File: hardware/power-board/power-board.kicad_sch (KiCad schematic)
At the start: 0 parts

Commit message: Segregated specific libs into shared libs
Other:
- added sheet BMS (bms.kicad_sch)
- added sheet Charger (charger.kicad_sch)
- added sheet Control (control.kicad_sch)
- added sheet Hotswap (hotswap.kicad_sch)
- added sheet Hotswap1 (hotswap.kicad_sch)
- added sheet Supplies (supplies.kicad_sch)

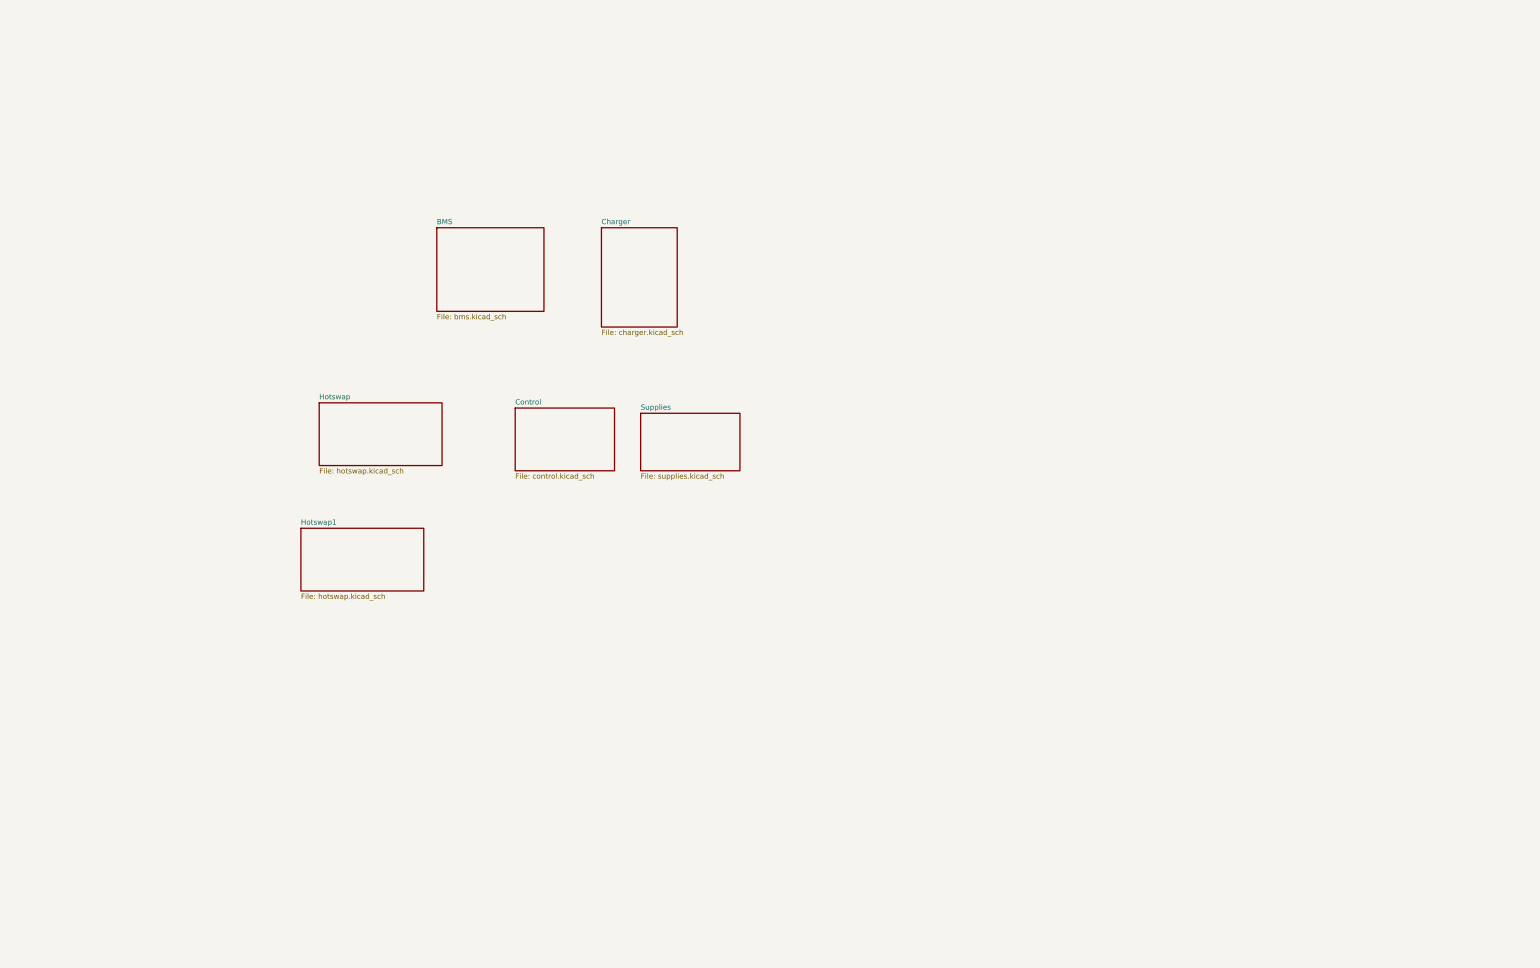
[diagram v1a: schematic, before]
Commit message: Added more ICs for power board
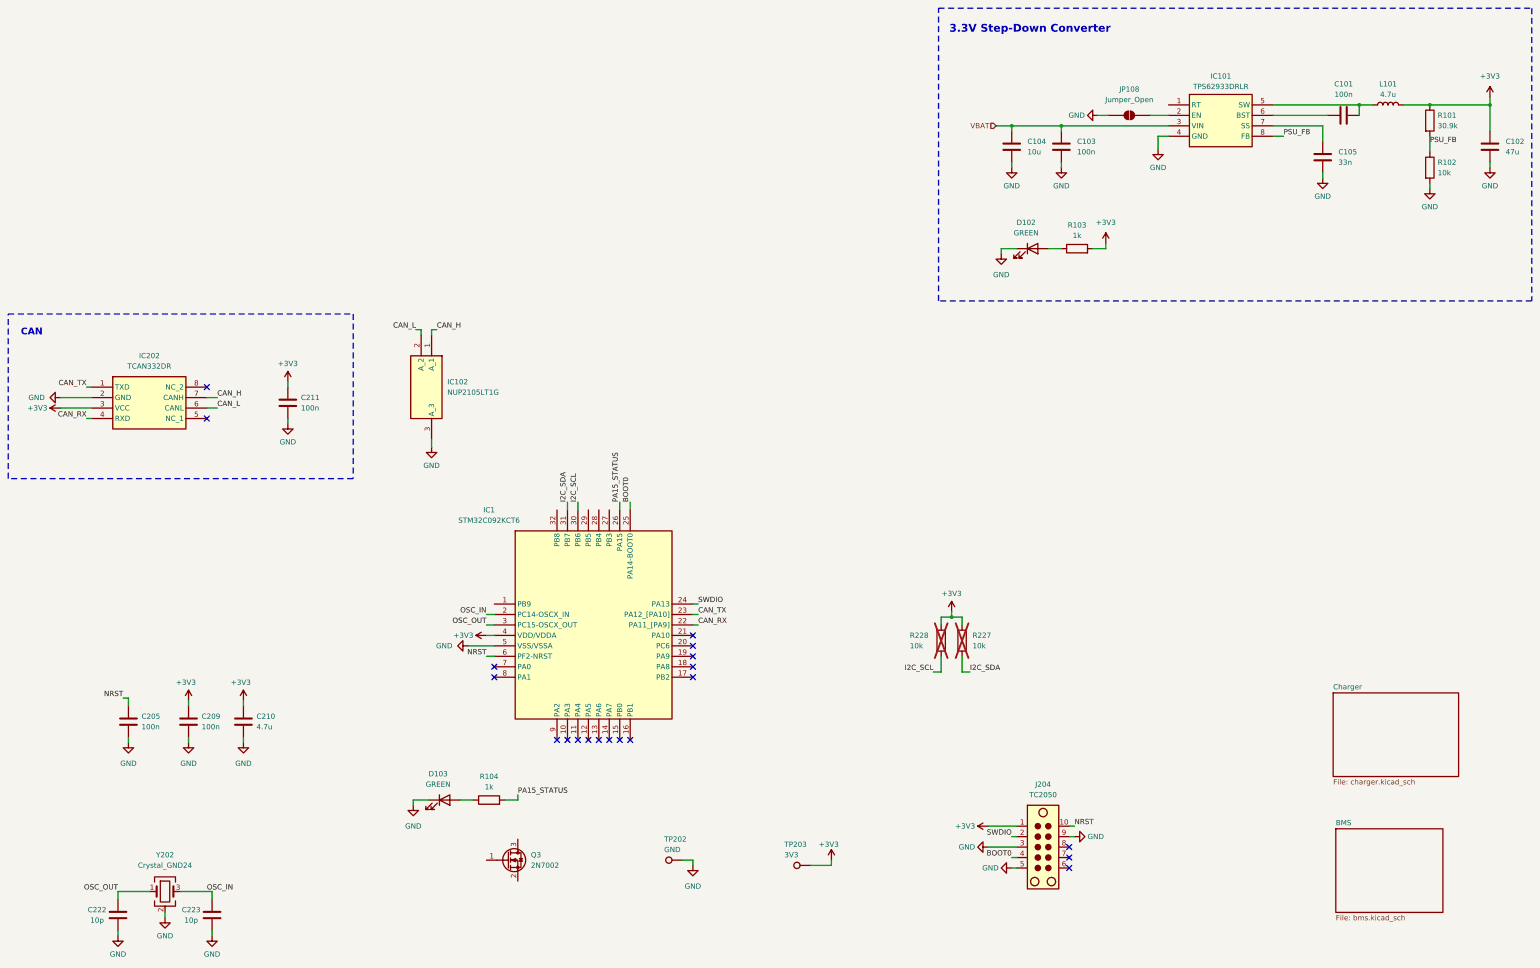
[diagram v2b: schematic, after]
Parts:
- added C101, C103, C205, C209, C211: 100n, Capacitor_SMD:C_0805_2012Metric, symbol Device:C
- added C102: 47u, Capacitor_SMD:C_0805_2012Metric, symbol Device:C
- added C104: 10u, Capacitor_SMD:C_0805_2012Metric, symbol Device:C
- added C105: 33n, Capacitor_SMD:C_0805_2012Metric, symbol Device:C
- added C210: 4.7u, Capacitor_SMD:C_0805_2012Metric, symbol Device:C
- added C222, C223: 10p, Capacitor_SMD:C_0805_2012Metric, symbol Device:C
- added D102, D103: GREEN, LED_SMD:LED_0805_2012Metric, symbol Device:LED
- added IC1: STM32C092KCT6, vector:QFP80P900X900X160-32N, symbol vector:STM32C092KCT6
- added IC101: TPS62933DRLR, vector:SOTFL50P160X60-8N, symbol vector:TPS62933DRLR
- added IC102: NUP2105LT1G, vector:SOT96P237X111-3N, symbol vector:NUP2105LT1G
- added IC202: TCAN332DR, vector:SOIC127P600X175-8N, symbol vector:TCAN332DR
- added J204: TC2050, Connector:Tag-Connect_TC2050-IDC-FP_2x05_P1.27mm_Vertical, symbol Connector:TC2050
- added JP108: Jumper_Open, Jumper:SolderJumper-2_P1.3mm_Open_Pad1.0x1.5mm, symbol Jumper:SolderJumper_2_Open
- added L101: 4.7u, symbol Device:L
- added Q3: 2N7002, Package_TO_SOT_SMD:SOT-23, symbol Transistor_FET:2N7002
- added R101: 30.9k, Resistor_SMD:R_0805_2012Metric, symbol Device:R
- added R102: 10k, Resistor_SMD:R_0805_2012Metric, symbol Device:R
- added R103, R104: 1k, Resistor_SMD:R_0603_1608Metric, symbol Device:R
- added R227, R228: 10k, Resistor_SMD:R_0603_1608Metric, symbol Device:R
- added TP202: GND, TestPoint:TestPoint_Pad_D2.0mm, symbol Connector:TestPoint
- added TP203: 3V3, TestPoint:TestPoint_Pad_D2.0mm, symbol Connector:TestPoint
- added Y202: Crystal_GND24, Crystal:Crystal_SMD_2016-4Pin_2.0x1.6mm, symbol Device:Crystal_GND24
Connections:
- new net: C101.1, IC101.6 (BST)
- new net: C101.2, IC101.5 (SW), L101.1
- new net: D102.2 (A), R103.1
- new net: IC101.2 (EN), JP108.2 (B)
- new net: C105.2, IC101.7 (SS)
- new net: D103.2 (A), R104.1
- new net +3V3: C102.2, C209.2, C210.2, C211.2, IC1.4 (VDD/VDDA), IC202.3 (VCC), J204.1, L101.2, R101.1, R103.2, R227.2, R228.1, TP203.1
- new net BOOT0: IC1.25 (PA14-BOOT0), J204.4
- new net CAN_H: IC102.1 (A_1), IC202.7 (CANH)
- new net CAN_L: IC102.2 (A_2), IC202.6 (CANL)
- new net CAN_RX: IC1.22 (PA11_[PA9]), IC202.4 (RXD)
- new net CAN_TX: IC1.23 (PA12_[PA10]), IC202.1 (TXD)
- new net GND: C102.1, C103.1, C104.1, C105.1, C205.1, C209.1, C210.1, C211.1, C222.1, C223.1, D102.1 (K), D103.1 (K), IC1.5 (VSS/VSSA), IC101.4 (GND), IC102.3 (A_3), IC202.2 (GND), J204.3, J204.5, J204.9, JP108.1 (A), R102.2, TP202.1, Y202.2 (G), Y202.4 (G)
- new net I2C_SCL: IC1.30 (PB6), R228.2
- new net I2C_SDA: IC1.31 (PB7), R227.1
- new net NRST: C205.2, IC1.6 (PF2-NRST), J204.10
- new net OSC_IN: C223.2, IC1.2 (PC14-OSCX_IN), Y202.3
- new net OSC_OUT: C222.2, IC1.3 (PC15-OSCX_OUT), Y202.1
- new net PA15_STATUS: IC1.26 (PA15), R104.2
- new net PSU_FB: IC101.8 (FB), R101.2, R102.1
- new net SWDIO: IC1.24 (PA13), J204.2
- new net VBAT: C103.2, C104.2, IC101.3 (VIN)
- no-connect marks 0 -> 20
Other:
- removed sheet Control
- removed sheet Hotswap
- removed sheet Hotswap1
- removed sheet Supplies
- note added: "3.3V Step-Down Converter"
- note added: "CAN"

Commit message: draw power board bms, charger and mcu circuits
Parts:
- added J501: CAN, Connector_JST:JST_GH_SM04B-GHS-TB_1x04-1MP_P1.25mm_Horizontal, symbol Connector_Generic:Conn_01x04
- added J502: SYSCTL, Connector_JST:JST_GH_SM06B-GHS-TB_1x06-1MP_P1.25mm_Horizontal, symbol Connector_Generic:Conn_01x06
- added R501, R503: 100k, Resistor_SMD:R_0603_1608Metric, symbol Device:R
- added R502: 100, Resistor_SMD:R_0603_1608Metric, symbol Device:R
- added R504, R505, R506, R507: 10k, Resistor_SMD:R_0603_1608Metric, symbol Device:R
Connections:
- net +3V3: now also R504.1, R505.1, R506.1, R507.1
- net CAN_H: now also J501.1 (Pin_1)
- net CAN_L: now also J501.2 (Pin_2)
- net GND: now also Q3.2 (S), J501.3 (Pin_3), J502.1 (Pin_1), R501.2, R503.2
- net REG1: now reaches IC101.2 (EN), JP108.2 (B)
- net 5V_PG: now reaches IC1.13 (PA6)
- net 5V_PG: now also J502.6 (Pin_6), R504.2
- net CM5_OFF: now reaches IC1.15 (PB0)
- net CM5_OFF: now also Q3.1 (G), R501.1
- net BMS_ALERT: now reaches IC1.16 (PB1)
- net BMS_ALERT: now also R506.2
- net CHG_INT: now reaches IC1.17 (PB2)
- net CHG_INT: now also R505.2
- net MCU_ESTOP_N: now reaches IC1.18 (PA8)
- net MCU_ESTOP_N: now also R502.1
- net SHUTDOWN_REQ_N: now reaches IC1.19 (PA9)
- net SHUTDOWN_REQ_N: now also J502.2 (Pin_2), R507.2
- net BTN_N: now reaches IC1.7 (PA0)
- net HALTED: now reaches IC1.8 (PA1)
- net HALTED: now also J502.3 (Pin_3), R503.1
- net 5V_EN: now reaches Q3.3 (D)
- net 5V_EN: now also J502.5 (Pin_5)
- net VBAT renamed BAT+
- new net ESTOP_N: J501.4 (Pin_4), J502.4 (Pin_4), R502.2
- no-connect marks 20 -> 17
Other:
- sheet BMS ports: added BAT+, BMS_ALERT, BTN_N, I2C_SCL, I2C_SDA, PACK+, REG1, TS2_WAKE; removed none
- sheet Charger ports: added CHG_INT, I2C_SCL, I2C_SDA, PACK+, TS2_WAKE; removed none
- note added: "Connectors"
- note added: "Power Control"
- moved on the sheet: Q3

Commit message: Reset annotations for power board
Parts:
- renumbered C222 to C101, C205 to C102, C209 to C103, C223 to C104, C210 to C105, C211 to C106, C104 to C107, C103 to C108, C105 to C109, C101 to C110, C102 to C111, D103 to D101, IC202 to IC101, IC1 to IC103, IC101 to IC104, J501 to J101, J502 to J102, J204 to J103, JP108 to JP101, Q3 to Q101, R501 to R101, R502 to R102, R503 to R103, R504 to R104, R505 to R105, R506 to R106, R507 to R107, R104 to R108, R228 to R109, R227 to R110, R103 to R111, R101 to R112, R102 to R113, TP202 to TP101, TP203 to TP102, Y202 to Y101

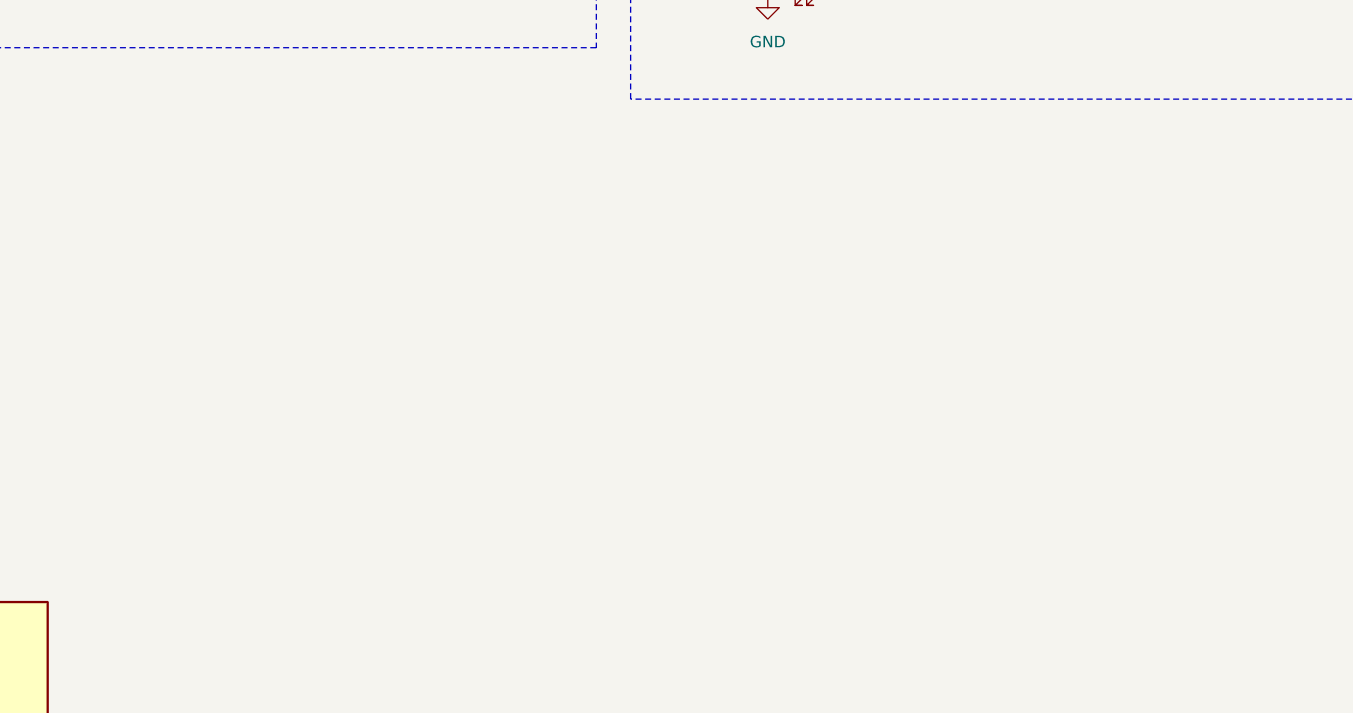
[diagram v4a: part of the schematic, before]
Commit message: power board: test points
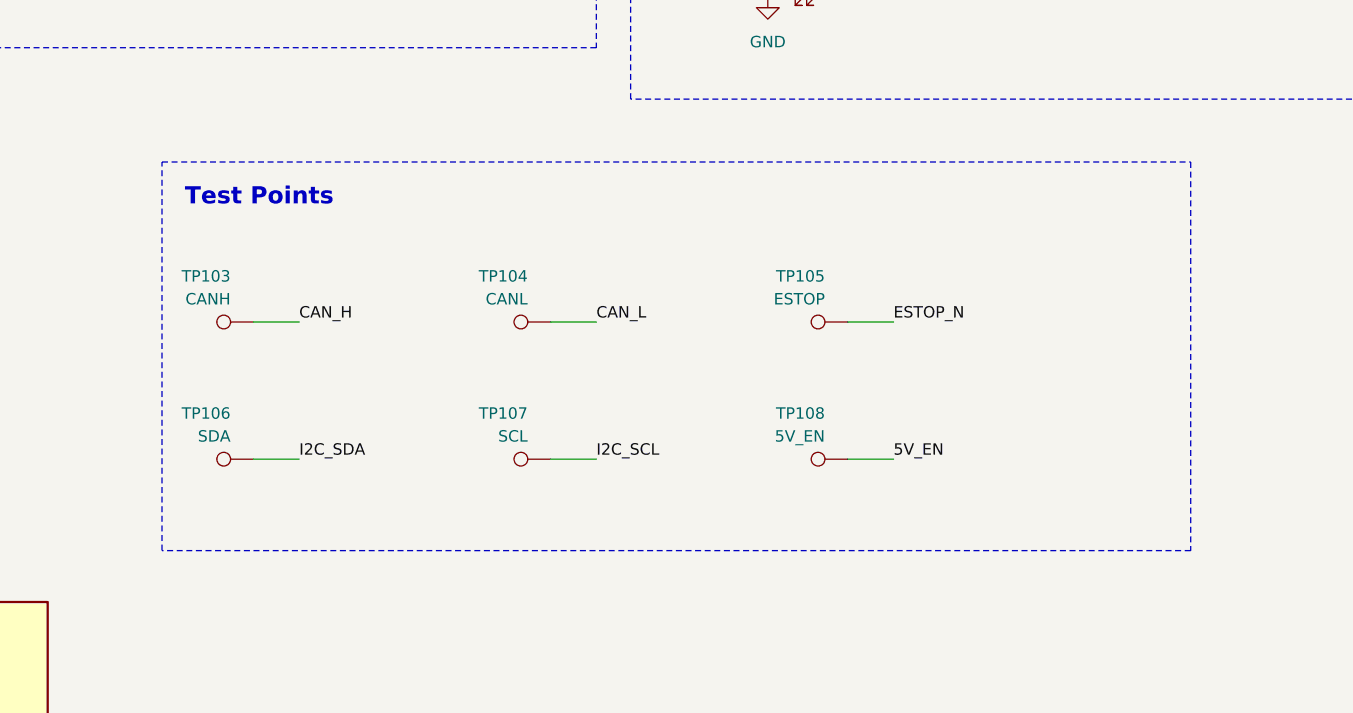
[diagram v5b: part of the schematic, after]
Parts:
- added TP103: CANH, TestPoint:TestPoint_Pad_D2.0mm, symbol Connector:TestPoint
- added TP104: CANL, TestPoint:TestPoint_Pad_D2.0mm, symbol Connector:TestPoint
- added TP105: ESTOP, TestPoint:TestPoint_Pad_D2.0mm, symbol Connector:TestPoint
- added TP106: SDA, TestPoint:TestPoint_Pad_D2.0mm, symbol Connector:TestPoint
- added TP107: SCL, TestPoint:TestPoint_Pad_D2.0mm, symbol Connector:TestPoint
- added TP108: 5V_EN, TestPoint:TestPoint_Pad_D2.0mm, symbol Connector:TestPoint
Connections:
- net 5V_EN: now also TP108.1
- net CAN_H: now also TP103.1
- net CAN_L: now also TP104.1
- net ESTOP_N: now also TP105.1
- net I2C_SCL: now also TP107.1
- net I2C_SDA: now also TP106.1
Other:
- note added: "Test Points"

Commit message: power board: amrm inductor, sot-223 for q204, 2.2k i2c pull-ups, 50 v charger caps, xh connectors
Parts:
- C101, C104: value 10p -> 18p
- J101: footprint Connector_JST:JST_GH_SM04B-GHS-TB_1x04-1MP_P1.25mm_Horizontal -> Connector_JST:JST_XH_S4B-XH-A-1_1x04_P2.50mm_Horizontal
- J102: footprint Connector_JST:JST_GH_SM06B-GHS-TB_1x06-1MP_P1.25mm_Horizontal -> Connector_JST:JST_XH_S6B-XH-A-1_1x06_P2.50mm_Horizontal
- L101: footprint (none) -> vector:INDPM116102X400N; Manufacturer_Part_Number (none) -> AMRM001010404R7MA1
- R109, R110: value 10k -> 2.2k
- Y101: Manufacturer_Part_Number (none) -> K2B400001210
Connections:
- no-connect marks 17 -> 18
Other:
- moved on the sheet: C101, C102, C103, C104, C105, D101, R108, R109, R110, TP101, TP102, Y101

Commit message: Updated sideboard PCB
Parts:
- L101: footprint vector:INDPM116102X400N -> vector:INDPM4441X200N; Manufacturer_Part_Number AMRM001010404R7MA1 -> SRP4020TA-4R7M
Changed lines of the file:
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@@
 			)
 		)
-		(property "Footprint" "vector:INDPM116102X400N"
+		(property "Footprint" "vector:INDPM4441X200N"
 			(at 367.03 41.91 0)
 			(hide yes)
@@
 			)
 		)
-		(property "Manufacturer_Part_Number" "AMRM001010404R7MA1"
+		(property "Manufacturer_Part_Number" "SRP4020TA-4R7M"
 			(at 367.03 41.91 0)
 			(hide yes)
